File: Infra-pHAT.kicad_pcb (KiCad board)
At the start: 2 copper layers, 65 x 30 mm, 25 parts, among them Q1 BC817, U1 CAT24C32WI-GT3

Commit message: Initial version SCH + PCM
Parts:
- removed ?: LOGO, logo:anavi-logo
- removed IRRX: TSOP34838, myfootprint:TSOP38X
- removed REF1, REF2, REF3, REF4: MountingHole_2.7mm_M2.5_DIN965_Pad, Mounting_Holes:MountingHole_2.7mm_M2.5_DIN965_Pad
- removed UART: CONN_01X04, Pin_Headers:Pin_Header_Straight_1x04
- added D1: 1N4148, Diodes_THT:D_T-1_P2.54mm_Vertical_AnodeUp, F.Cu at (129.2, 110.7)
- added IRRX1: TSOP34838, myfootprint:TSOP38X, F.Cu at (153.4, 124.2)
- added J1: CONN_01X03, myfootprint:KLEMA_1x3, F.Cu at (122.3, 130.5)
- added P1: RAS-05-15, myfootprint:RAS-05-15, F.Cu at (113.4, 107.6)
- added Q2: BC817-40, TO_SOT_Packages_SMD:SOT-23, F.Cu at (135.6, 119.1)
- added R8: 2.7k, Resistors_SMD:R_0603_HandSoldering, F.Cu at (140.7, 109.4)
- added R9: 27k, Resistors_SMD:R_0603_HandSoldering, F.Cu at (130.5, 120.3)
- added REF**: MountingHole_2.7mm_M2.5_DIN965_Pad, Mounting_Holes:MountingHole_2.7mm_M2.5_DIN965_Pad, F.Cu at (161.6, 103.8)
- added REF**: MountingHole_2.7mm_M2.5_DIN965_Pad, Mounting_Holes:MountingHole_2.7mm_M2.5_DIN965_Pad, F.Cu at (103.6, 103.6)
- added REF**: MountingHole_2.7mm_M2.5_DIN965_Pad, Mounting_Holes:MountingHole_2.7mm_M2.5_DIN965_Pad, F.Cu at (161.6, 126.6)
- added REF**: MountingHole_2.7mm_M2.5_DIN965_Pad, Mounting_Holes:MountingHole_2.7mm_M2.5_DIN965_Pad, F.Cu at (103.6, 126.6)
- IRTX1, IRTX2: footprint LEDs:LED-5MM -> LEDs:LED_D5.0mm
- JP1: footprint Pin_Headers:Pin_Header_Straight_1x02 -> Pin_Headers:Pin_Header_Straight_1x02_Pitch1.00mm
- RASP_CONN1: footprint Pin_Headers:Pin_Header_Straight_2x20 -> myfootprint:Pin_Header_Straight_2x20
- SENS1, SENS2, SENS3: footprint Pin_Headers:Pin_Header_Straight_1x04 -> Pin_Headers:Pin_Header_Straight_1x04_Pitch1.00mm
- moved C1 88.5 mm to (130.5, 122.9), turned to 180 degrees
- moved R3 69.5 mm to (140.7, 112.7), turned to 0 degrees
- moved R2 68.9 mm to (140.7, 115.3), turned to 0 degrees
- moved R1 68.2 mm to (150.8, 122.9), turned to 0 degrees
- moved SENS3 67.7 mm to (133.0, 125.4), turned to 0 degrees
- moved SENS1 65.5 mm to (129.5, 125.4), turned to 0 degrees
- moved SENS2 61.9 mm to (136.6, 125.4), turned to 0 degrees
- moved JP1 60.7 mm to (155.9, 121.6)
- moved IRTX1 56.5 mm to (105.1, 118.1), turned to 180 degrees
- moved IRTX2 50.2 mm to (105.1, 110.9), turned to 180 degrees
- moved U1 44.5 mm to (160.5, 117.8), turned to 180 degrees
- moved R6 44.4 mm to (140.7, 120.3), turned to 180 degrees
- moved R7 39.8 mm to (140.7, 117.8), turned to 180 degrees
- moved R5 39.2 mm to (145.7, 122.9), turned to 180 degrees
- moved C2 37.4 mm to (145.7, 126.7)
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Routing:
- net GND: track 8.40 -> 181.3 mm
- net Net-(IRTX1-Pad1): track 7.02 -> 56.2 mm
- net Net-(IRRX1-Pad1): track 45.1 -> 80.4 mm
- net Net-(D1-Pad2): track 0.00 -> 26.5 mm
- net +5V: track 17.5 -> 40.4 mm, vias 1 -> 0
- net Net-(J1-Pad2): track 0.00 -> 20.3 mm
- net Net-(R6-Pad2): track 39.0 -> 56.9 mm, vias 3 -> 0
- net Net-(Q2-Pad1): track 0.00 -> 16.6 mm
- net Net-(J1-Pad1): track 0.00 -> 15.8 mm
- net /RXD: track 11.6 -> 0.00 mm
- net /TXD: track 11.6 -> 0.00 mm
- net Net-(JP1-Pad1): track 10.1 -> 21.4 mm
- net Net-(R7-Pad2): track 45.2 -> 54.7 mm, vias 1 -> 0
- net Net-(R3-Pad2): track 35.1 -> 26.8 mm
- net Net-(C2-Pad1): track 9.96 -> 16.9 mm
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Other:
- board size 65 x 30 mm -> 65 x 30.1 mm
- net class vcc removed
- rule trace_min: 0.25 -> 0.254
- rule via_min_drill: 0.3 -> 0.35
- rule via_min_size: 0.4 -> 0.7
- board text removed: "100nF"
- board text removed: "10K"
- board text removed: "1K"
- board text removed: "3.3V TX RX GND"
- board text removed: "3x I2C"
- board text removed: "4,7K"
- board text removed: "4,7pF"
- board text removed: "470"
- board text removed: "ANAVI Infrared pHAT"
- board text removed: "BC817"
- board text removed: "Made in Plovdiv, Bulgaria, EU"
- board text removed: "Rev 1.0 (c) 2017"
- board text removed: "SDA SCL GND 3.3V"
- board text removed: "http://anavi.technology"

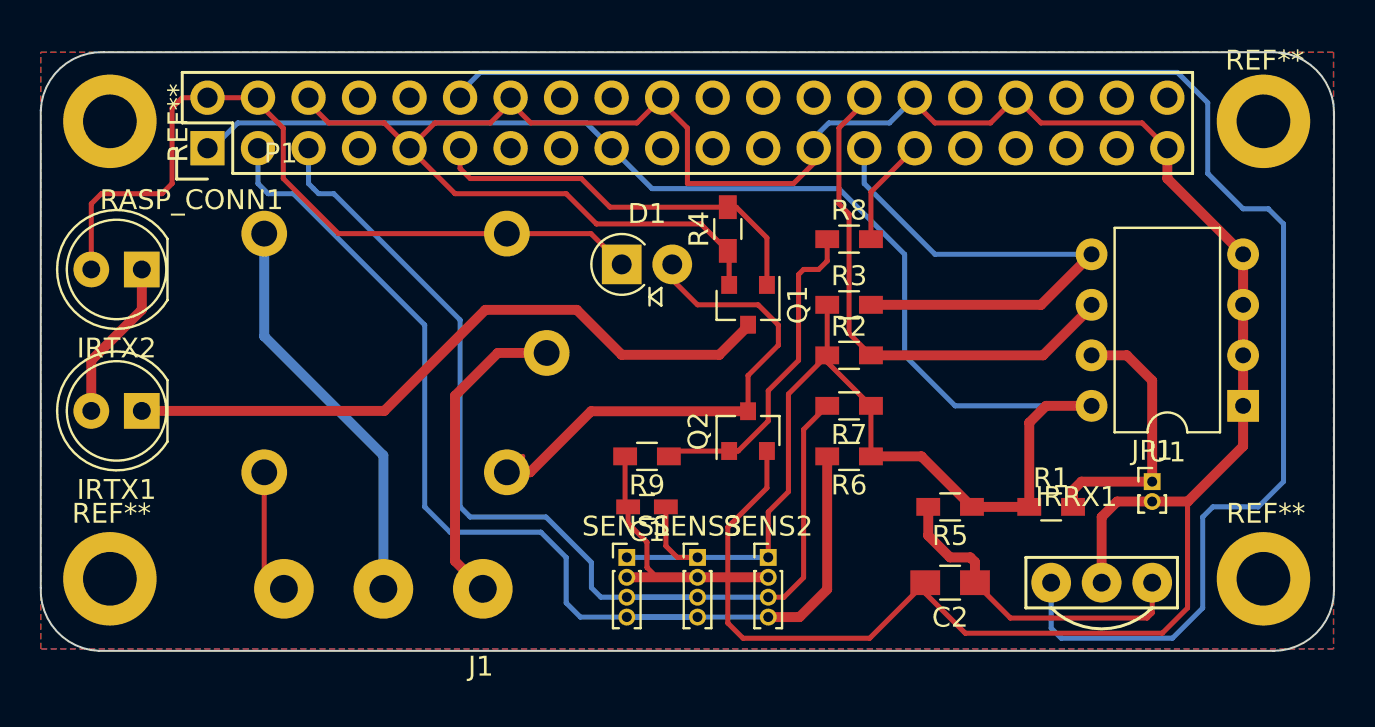
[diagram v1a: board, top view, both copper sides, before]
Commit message: Updated PCB with better tracks and oshpark kicad rules
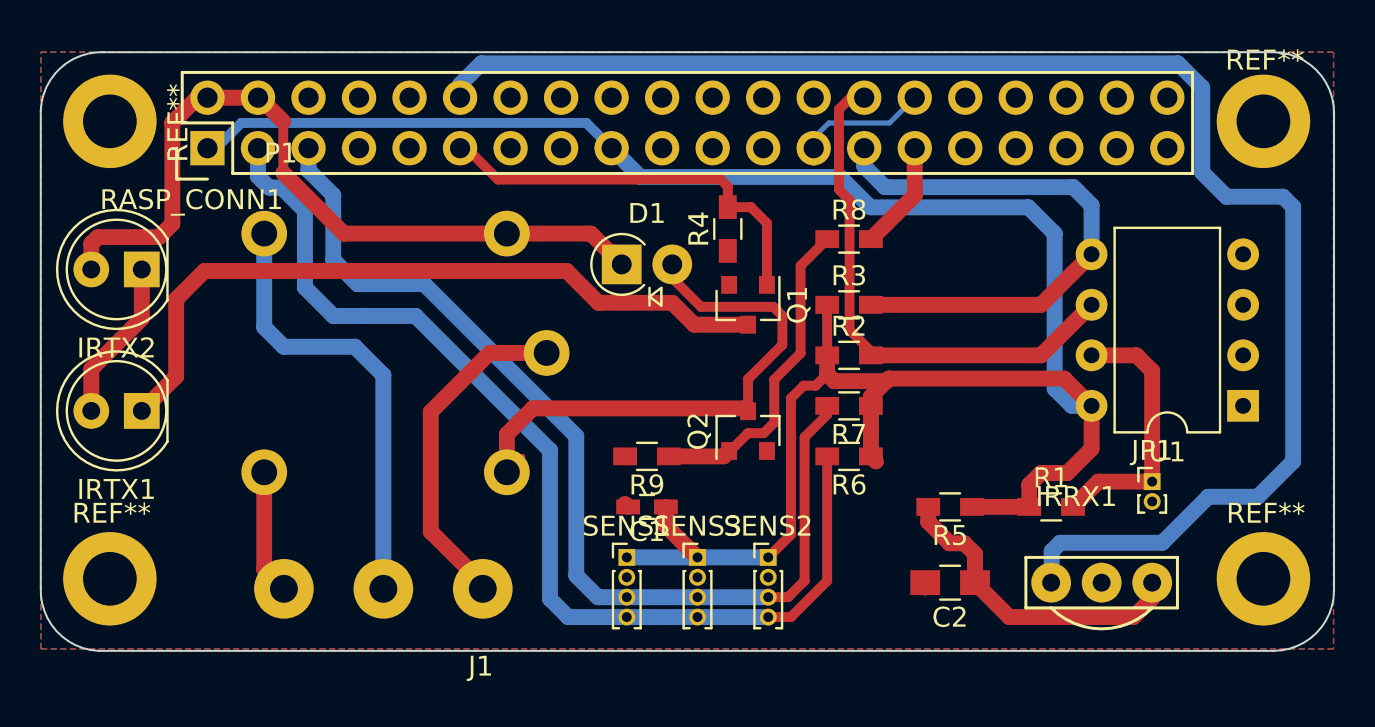
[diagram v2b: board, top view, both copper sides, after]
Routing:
- net GND: track 181.3 -> 10.4 mm
- net +5V: track 40.4 -> 60.4 mm
- net Net-(IRTX1-Pad1): track 56.2 -> 36.9 mm
- net Net-(R2-Pad2): track 38.5 -> 27.0 mm
- net Net-(JP1-Pad1): track 21.4 -> 13.4 mm
- net Net-(J1-Pad3): track 6.27 -> 13.3 mm
- net Net-(IRTX1-Pad2): track 14.3 -> 8.16 mm
- net Net-(R7-Pad2): track 54.7 -> 50.6 mm
- net Net-(R6-Pad2): track 56.9 -> 53.4 mm
- net Net-(IRRX1-Pad1): track 80.4 -> 77.1 mm
- net Net-(D1-Pad2): track 26.5 -> 29.0 mm
- net Net-(J1-Pad2): track 20.3 -> 22.4 mm
- net Net-(J1-Pad1): track 15.8 -> 17.0 mm
- net +3V3: track 109.6 -> 110.8 mm
- net Net-(R3-Pad2): track 26.8 -> 27.8 mm
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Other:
- net class Default: clearance 0.254 -> 0.1524; trace_width 0.5 -> 0.1524; via_dia 0.85 -> 0.6858; via_drill 0.4 -> 0.3302
- rule trace_clearance: 0.254 -> 0.1524
- rule trace_min: 0.254 -> 0.1524
- rule via_min_drill: 0.35 -> 0.3302
- rule via_min_size: 0.7 -> 0.6858

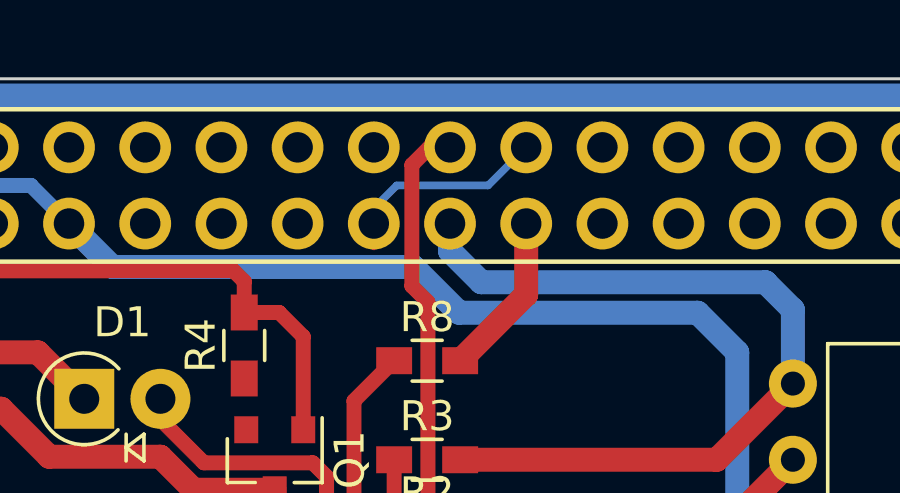
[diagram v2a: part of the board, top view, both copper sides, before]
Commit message: Fix on back layer GND25-30 pin
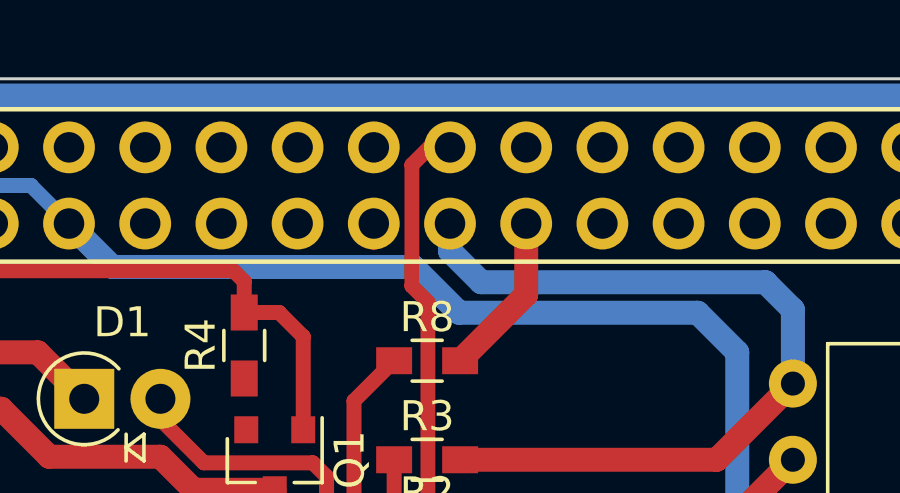
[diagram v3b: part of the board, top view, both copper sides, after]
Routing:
- net GND: track 10.4 -> 4.46 mm
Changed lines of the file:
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@@
   (general
     (links 67)
-    (no_connects 7)
+    (no_connects 8)
     (area 88.500229 88.500228 176.701172 133.5326)
     (thickness 1.6002)
     (drawings 8)
-    (tracks 241)
+    (tracks 238)
     (zones 0)
     (modules 29)
@@
   (layers
     (0 F.Cu signal)
-    (31 B.Cu signal hide)
+    (31 B.Cu signal)
     (34 B.Paste user)
     (35 F.Paste user)
@@
   (segment (start 143.9672 102.3112) (end 143.9672 102.5652) (width 0.254) (layer F.Cu) (net 2))
   (segment (start 138.8872 104.8512) (end 138.8872 104.3432) (width 0.254) (layer B.Cu) (net 2))
-  (segment (start 138.8872 104.3432) (end 139.6492 103.5812) (width 0.254) (layer B.Cu) (net 2))
-  (segment (start 142.6972 103.5812) (end 143.9672 102.3112) (width 0.254) (layer B.Cu) (net 2))
-  (segment (start 139.6492 103.5812) (end 142.6972 103.5812) (width 0.254) (layer B.Cu) (net 2))
   (segment (start 138.8872 104.8512) (end 138.8872 105.6132) (width 0.254) (layer F.Cu) (net 2))
   (segment (start 131.2672 102.3112) (end 131.2672 102.5652) (width 0.254) (layer F.Cu) (net 2))
